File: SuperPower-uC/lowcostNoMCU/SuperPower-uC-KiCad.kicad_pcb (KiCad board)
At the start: 2 copper layers, 78.4 x 25.5 mm, 63 parts, among them J2 Thermistor, J3 USB_B_Micro, J4 Solar in, J5 Conn_01x08_Female, J6 Conn_01x12_Female, Q1 2N7002, Q2 2N7002, Q3 AO3401A, Q4 AO3401A, Q7 2N7002, U1 FS312F-G, U10 FP6291LR, U11 ME6210A33P, U12 ME6210A33P, U2 FS8205A, U3 LC709203FQH, U4 TP4056, U7 PCF8563T, U8 XC6206P332MR, U9 TCA6408A, Y2 32.768KHz

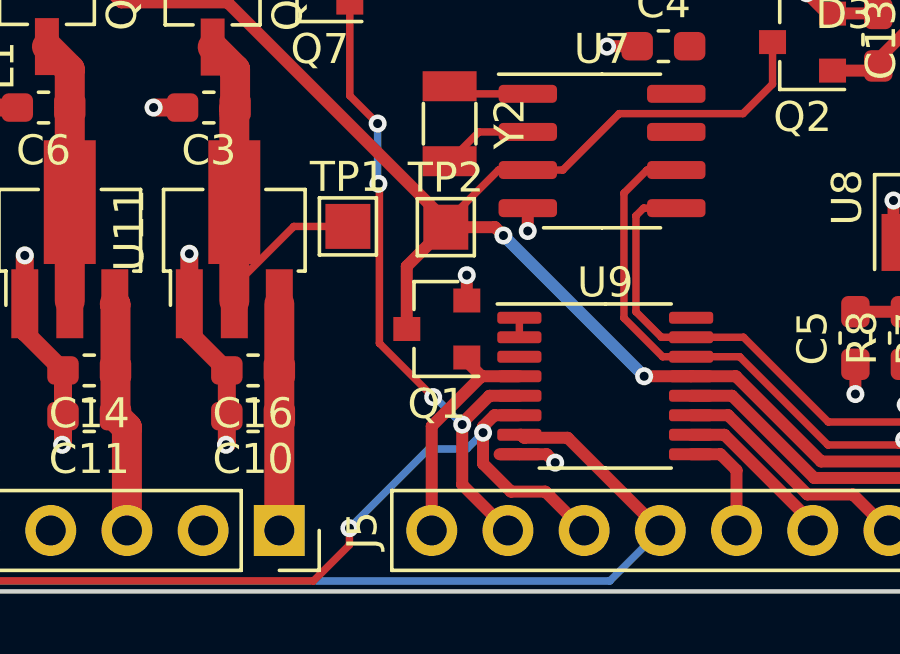
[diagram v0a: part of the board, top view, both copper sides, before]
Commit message: fixed drc and erc errors
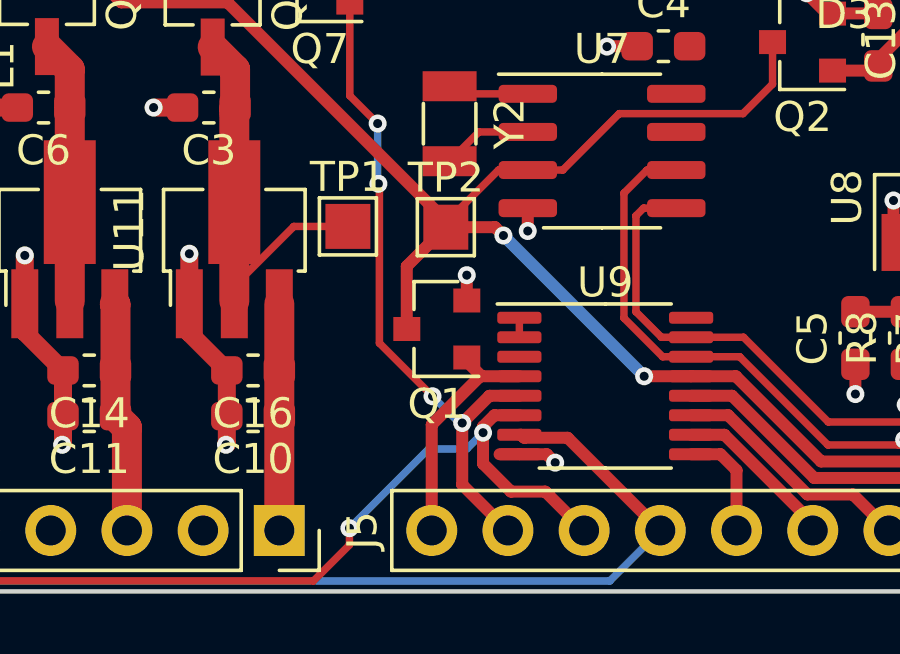
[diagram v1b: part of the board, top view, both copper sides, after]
